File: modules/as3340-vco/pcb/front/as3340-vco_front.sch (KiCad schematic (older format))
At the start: 41 parts, among them J1 CV1, J2 CV2, J3 LINEAR, J4 TRIANGLE, J5 SAWTOOTH, J6 PULSE, J7 Conn_01x09, U1 TL074

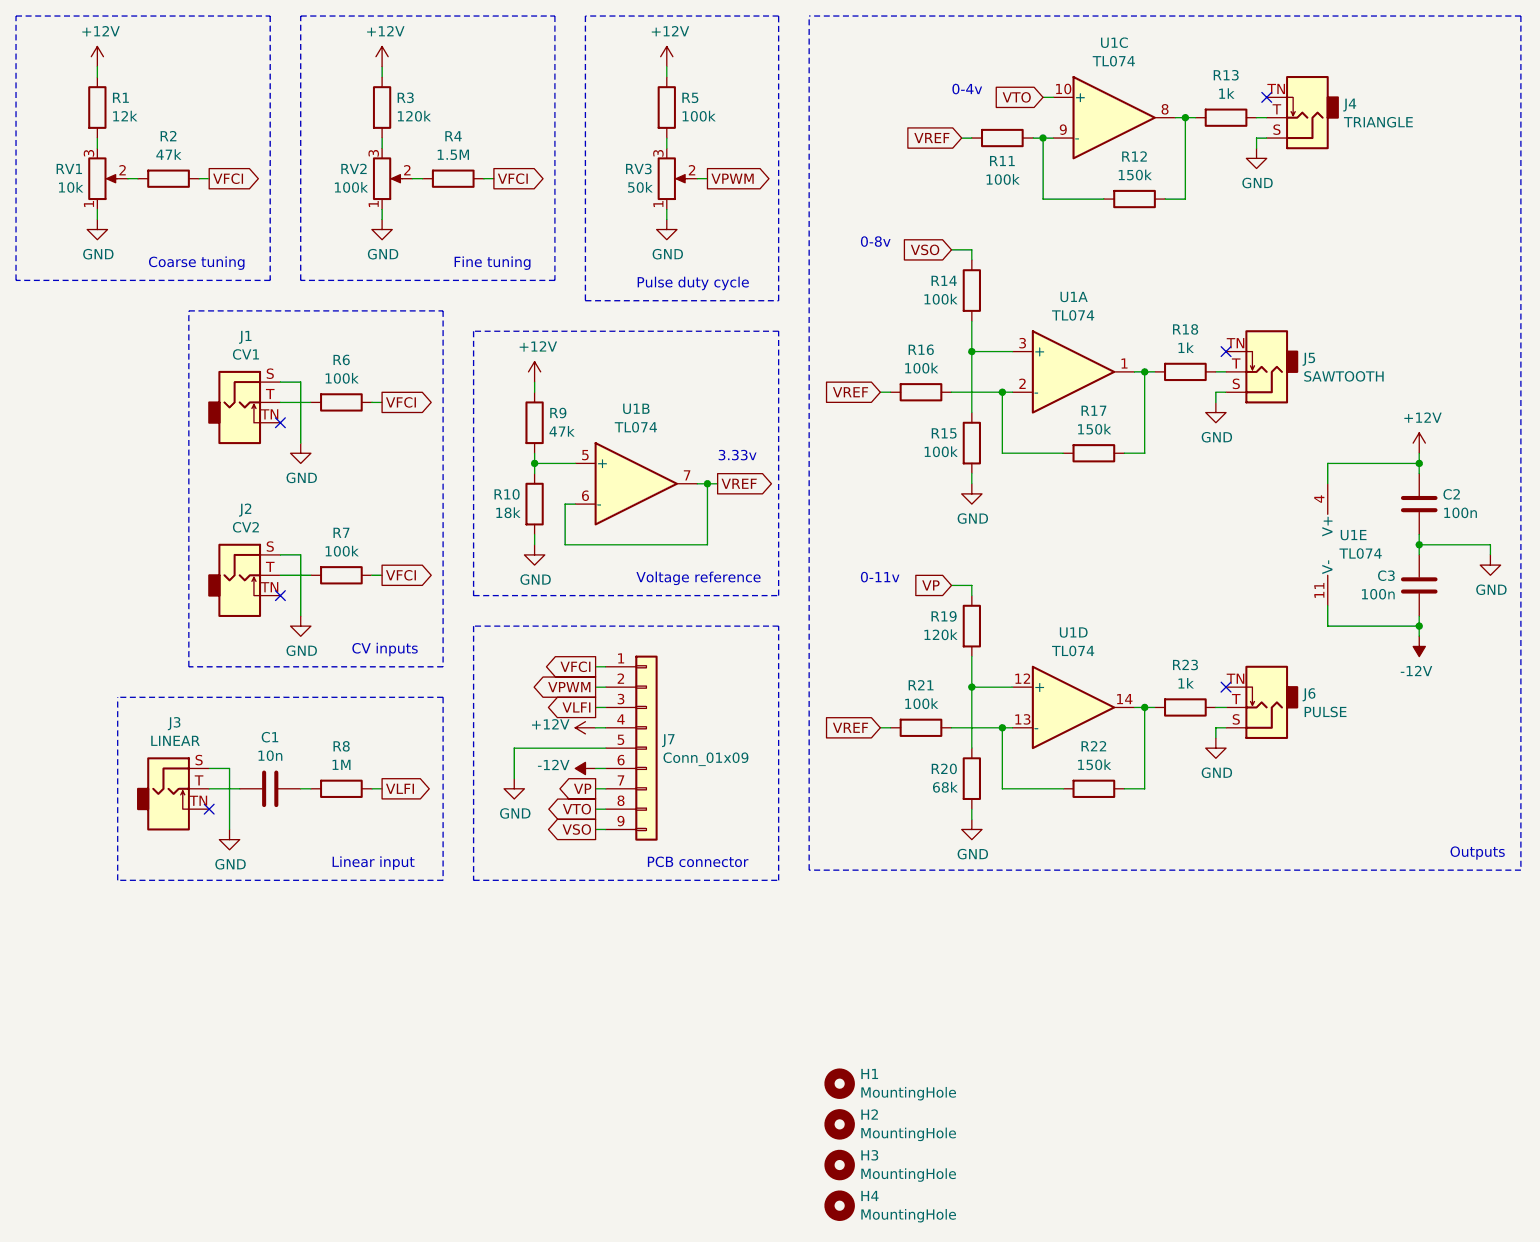
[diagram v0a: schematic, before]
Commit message: modules: as3340-vco: fix references
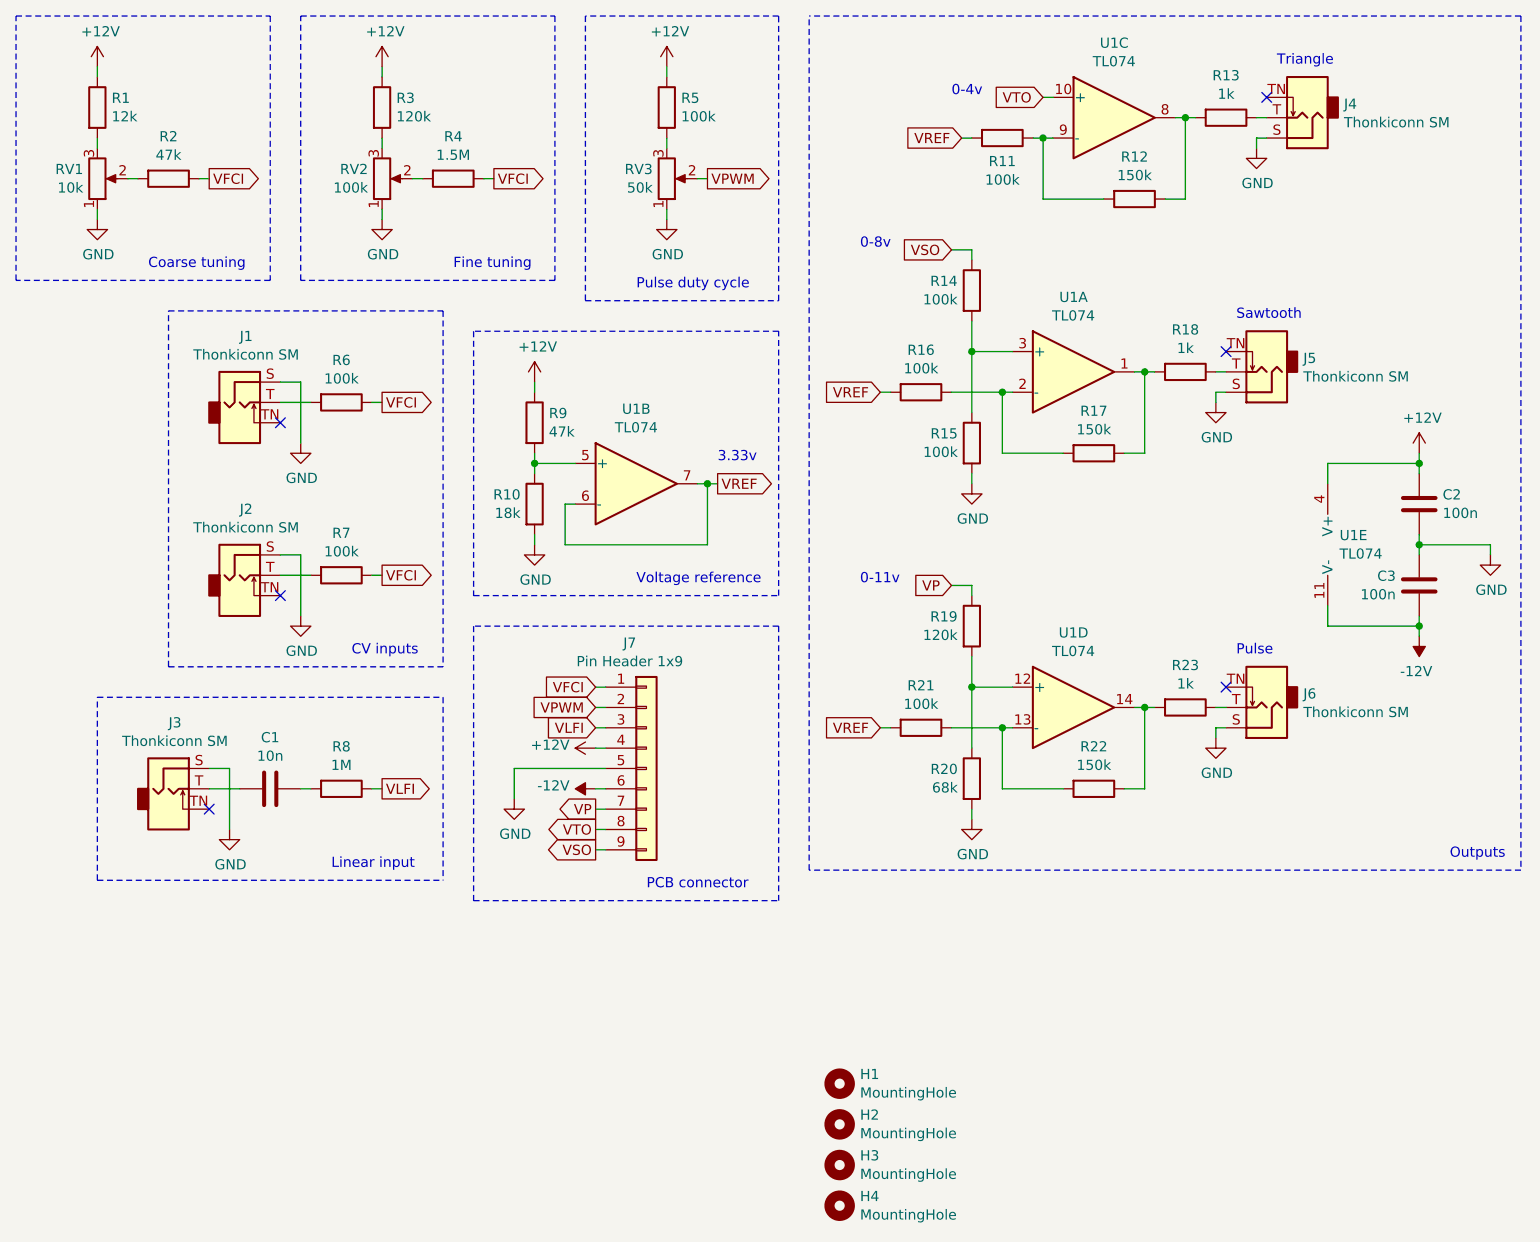
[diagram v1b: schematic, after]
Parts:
- J1: value CV1 -> Thonkiconn SM
- J2: value CV2 -> Thonkiconn SM
- J3: value LINEAR -> Thonkiconn SM
- J4: value TRIANGLE -> Thonkiconn SM
- J5: value SAWTOOTH -> Thonkiconn SM
- J6: value PULSE -> Thonkiconn SM
- J7: value Conn_01x09 -> Pin Header 1x9
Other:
- note added: "Pulse"
- note added: "Sawtooth"
- note added: "Triangle"
- moved on the sheet: J7
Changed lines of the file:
@@
 encoding utf-8
 Sheet 1 1
-Title "as3340-vco front board"
+Title "as3340-vco front"
 Date "2021-12-14"
 Rev "1.0"
@@
 Comment4 ""
 $EndDescr
-Text GLabel 5100 5350 0    50   Output ~ 0
+Text GLabel 5100 5450 0    50   Output ~ 0
 VTO
 $Comp
@@
 	1    0    0    -1
 $EndComp
-Text GLabel 5100 5450 0    50   Output ~ 0
+Text GLabel 5100 5550 0    50   Output ~ 0
 VSO
-Text GLabel 5100 4650 0    50   Output ~ 0
+Text GLabel 5100 4750 0    50   Input ~ 0
 VFCI
 $Comp
 L power:-12V #PWR0121
 U 1 1 61894347
-P 5100 5150
-F 0 "#PWR0121" H 5100 5250 50  0001 C CNN
-F 1 "-12V" V 5115 5278 50  0000 L CNN
-F 2 "" H 5100 5150 50  0001 C CNN
-F 3 "" H 5100 5150 50  0001 C CNN
-	1    5100 5150
+P 5100 5250
+F 0 "#PWR0121" H 5100 5350 50  0001 C CNN
+F 1 "-12V" V 5115 5378 50  0000 L CNN
+F 2 "" H 5100 5250 50  0001 C CNN
+F 3 "" H 5100 5250 50  0001 C CNN
+	1    5100 5250
 	0    -1   -1   0
 $EndComp
@@
 L power:+12V #PWR0124
 U 1 1 61896B8D
-P 5100 4950
-F 0 "#PWR0124" H 5100 4800 50  0001 C CNN
-F 1 "+12V" V 5115 5078 50  0000 L CNN
-F 2 "" H 5100 4950 50  0001 C CNN
-F 3 "" H 5100 4950 50  0001 C CNN
-	1    5100 4950
+P 5100 5050
+F 0 "#PWR0124" H 5100 4900 50  0001 C CNN
+F 1 "+12V" V 5115 5178 50  0000 L CNN
+F 2 "" H 5100 5050 50  0001 C CNN
+F 3 "" H 5100 5050 50  0001 C CNN
+	1    5100 5050
 	0    -1   -1   0
 $EndComp
@@
 L power:GND #PWR0125
 U 1 1 618ABB8E
-P 4700 5200
-F 0 "#PWR0125" H 4700 4950 50  0001 C CNN
-F 1 "GND" H 4705 5027 50  0000 C CNN
-F 2 "" H 4700 5200 50  0001 C CNN
-F 3 "" H 4700 5200 50  0001 C CNN
-	1    4700 5200
-	1    0    0    -1
-$EndComp
-Text Notes 5350 5650 0    50   ~ 0
+P 4700 5300
+F 0 "#PWR0125" H 4700 5050 50  0001 C CNN
+F 1 "GND" H 4705 5127 50  0000 C CNN
+F 2 "" H 4700 5300 50  0001 C CNN
+F 3 "" H 4700 5300 50  0001 C CNN
+	1    4700 5300
+	1    0    0    -1
+$EndComp
+Text Notes 5350 5750 0    50   ~ 0
 PCB connector
 Wire Notes Line
@@
 P 3350 3350
 F 0 "J1" H 3382 3675 50  0000 C CNN
-F 1 "CV1" H 3382 3584 50  0000 C CNN
+F 1 "Thonkiconn SM" H 3382 3584 50  0000 C CNN
 F 2 "eurorack:Jack_3.5mm_QingPu_WQP-PJ398SM_Vertical" H 3350 3350 50  0001 C CNN
 F 3 "~" H 3350 3350 50  0001 C CNN
@@
 P 3350 4200
 F 0 "J2" H 3382 4525 50  0000 C CNN
-F 1 "CV2" H 3382 4434 50  0000 C CNN
+F 1 "Thonkiconn SM" H 3382 4434 50  0000 C CNN
 F 2 "eurorack:Jack_3.5mm_QingPu_WQP-PJ398SM_Vertical" H 3350 4200 50  0001 C CNN
 F 3 "~" H 3350 4200 50  0001 C CNN
@@
 Text Notes 3900 4600 0    50   ~ 0
 CV inputs
-Wire Notes Line
-	3100 2900 4350 2900
 $Comp
 L Device:C C2
@@
 Text Notes 9300 5600 0    50   ~ 0
 Outputs
-Text GLabel 5100 5250 0    50   Output ~ 0
+Text GLabel 5100 5350 0    50   Output ~ 0
 VP
-Text GLabel 5100 4750 0    50   Output ~ 0
+Text GLabel 5100 4850 0    50   Input ~ 0
 VPWM
-Text GLabel 5100 4850 0    50   Output ~ 0
+Text GLabel 5100 4950 0    50   Input ~ 0
 VLFI
 $Comp
@@
 P 8600 1950
 F 0 "J4" H 8420 1883 50  0000 R CNN
-F 1 "TRIANGLE" H 8420 1974 50  0000 R CNN
+F 1 "Thonkiconn SM" H 8420 1974 50  0000 R CNN
 F 2 "eurorack:Jack_3.5mm_QingPu_WQP-PJ398SM_Vertical" H 8600 1950 50  0001 C CNN
 F 3 "~" H 8600 1950 50  0001 C CNN
@@
 P 8400 3200
 F 0 "J5" H 8220 3133 50  0000 R CNN
-F 1 "SAWTOOTH" H 8220 3224 50  0000 R CNN
+F 1 "Thonkiconn SM" H 8220 3224 50  0000 R CNN
 F 2 "eurorack:Jack_3.5mm_QingPu_WQP-PJ398SM_Vertical" H 8400 3200 50  0001 C CNN
 F 3 "~" H 8400 3200 50  0001 C CNN
@@
 P 8400 4850
 F 0 "J6" H 8220 4783 50  0000 R CNN
-F 1 "PULSE" H 8220 4874 50  0000 R CNN
+F 1 "Thonkiconn SM" H 8220 4874 50  0000 R CNN
 F 2 "eurorack:Jack_3.5mm_QingPu_WQP-PJ398SM_Vertical" H 8400 4850 50  0001 C CNN
 F 3 "~" H 8400 4850 50  0001 C CNN
@@
 P 3000 5250
 F 0 "J3" H 3032 5575 50  0000 C CNN
-F 1 "LINEAR" H 3032 5484 50  0000 C CNN
+F 1 "Thonkiconn SM" H 3032 5484 50  0000 C CNN
 F 2 "eurorack:Jack_3.5mm_QingPu_WQP-PJ398SM_Vertical" H 3000 5250 50  0001 C CNN
 F 3 "~" H 3000 5250 50  0001 C CNN
@@
 Text Notes 3800 5650 0    50   ~ 0
 Linear input
-Wire Notes Line
-	4350 4800 2750 4800
 Text GLabel 5650 2250 2    50   Output ~ 0
 VPWM
@@
 	4350 2900 4350 4650
 Wire Notes Line
-	4350 4650 3100 4650
-Wire Notes Line
-	3100 4650 3100 2900
+	3000 4650 3000 2900
 Wire Notes Line
 	4350 4800 4350 5700
 Wire Notes Line
-	4350 5700 2750 5700
-Wire Notes Line
-	2750 5700 2750 4800
+	2650 5700 2650 4800
 Wire Wire Line
 	9500 4100 9500 4050
@@
 L Connector_Generic:Conn_01x09 J7
 U 1 1 61BADC36
-P 5350 5050
-F 0 "J7" H 5430 5092 50  0000 L CNN
-F 1 "Conn_01x09" H 5430 5001 50  0000 L CNN
-F 2 "Connector_PinHeader_2.54mm:PinHeader_1x09_P2.54mm_Vertical" H 5350 5050 50  0001 C CNN
-F 3 "~" H 5350 5050 50  0001 C CNN
-	1    5350 5050
-	1    0    0    -1
-$EndComp
-Wire Wire Line
-	4700 5200 4700 5050
-Wire Wire Line
-	4700 5050 5150 5050
-Wire Wire Line
-	5100 5150 5150 5150
+P 5350 5150
+F 0 "J7" H 5268 5767 50  0000 C CNN
+F 1 "Pin Header 1x9" H 5268 5676 50  0000 C CNN
+F 2 "Connector_PinHeader_2.54mm:PinHeader_1x09_P2.54mm_Vertical" H 5350 5150 50  0001 C CNN
+F 3 "~" H 5350 5150 50  0001 C CNN
+	1    5350 5150
+	1    0    0    -1
+$EndComp
+Wire Wire Line
+	4700 5300 4700 5150
+Wire Wire Line
+	4700 5150 5150 5150
 Wire Wire Line
 	5100 5250 5150 5250
@@
 	5100 5450 5150 5450
 Wire Wire Line
+	5100 5550 5150 5550
+Wire Wire Line
+	5100 5050 5150 5050
+Wire Wire Line
+	5100 4750 5150 4750
+Wire Wire Line
+	5100 4850 5150 4850
+Wire Wire Line
 	5100 4950 5150 4950
-Wire Wire Line
-	5100 4650 5150 4650
-Wire Wire Line
-	5100 4750 5150 4750
-Wire Wire Line
-	5100 4850 5150 4850
-Wire Notes Line
-	4500 4450 4500 5700
-Wire Notes Line
-	4500 5700 6000 5700
-Wire Notes Line
-	6000 5700 6000 4450
+Wire Notes Line
+	4500 5800 6000 5800
+Text Notes 8450 1700 0    50   ~ 0
+Triangle
+Text Notes 8250 2950 0    50   ~ 0
+Sawtooth
+Text Notes 8250 4600 0    50   ~ 0
+Pulse
+Wire Notes Line
+	2650 5700 4350 5700
+Wire Notes Line
+	2650 4800 4350 4800
+Wire Notes Line
+	3000 4650 4350 4650
+Wire Notes Line
+	3000 2900 4350 2900
+Wire Notes Line
+	4500 4450 4500 5800
+Wire Notes Line
+	6000 4450 6000 5800
 $EndSCHEMATC
